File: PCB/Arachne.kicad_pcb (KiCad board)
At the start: 2 copper layers, 100 x 100 mm, 276 parts, among them J201 SW2, J301 SW2, J401 SW2, J501 SW2, J601 SW2, J701 SW2, J801 V_IN, J901 USB_B, J902 PROG_CONN_STM_6p, J903 DBG_UART, M201 Stepper_Motor_bipolar, M301 Stepper_Motor_bipolar, M401 Stepper_Motor_bipolar, M501 Stepper_Motor_bipolar, M601 Stepper_Motor_bipolar, M701 Stepper_Motor_bipolar, Q801 AOD4189, SW101 SW_Push, U101 STM32L452CEUx, U102 WS2818B, U201 L6470_HTSSOP28, U301 L6470_HTSSOP28, U401 L6470_HTSSOP28, U501 L6470_HTSSOP28, U601 L6470_HTSSOP28, U701 L6470_HTSSOP28, U801 ACS712xLCTR-20A, U802 NCP1117-5.0_SOT223, U803 L5973D, U804 NCP1117-3.3_SOT223, U901 USBLC6-2SC6

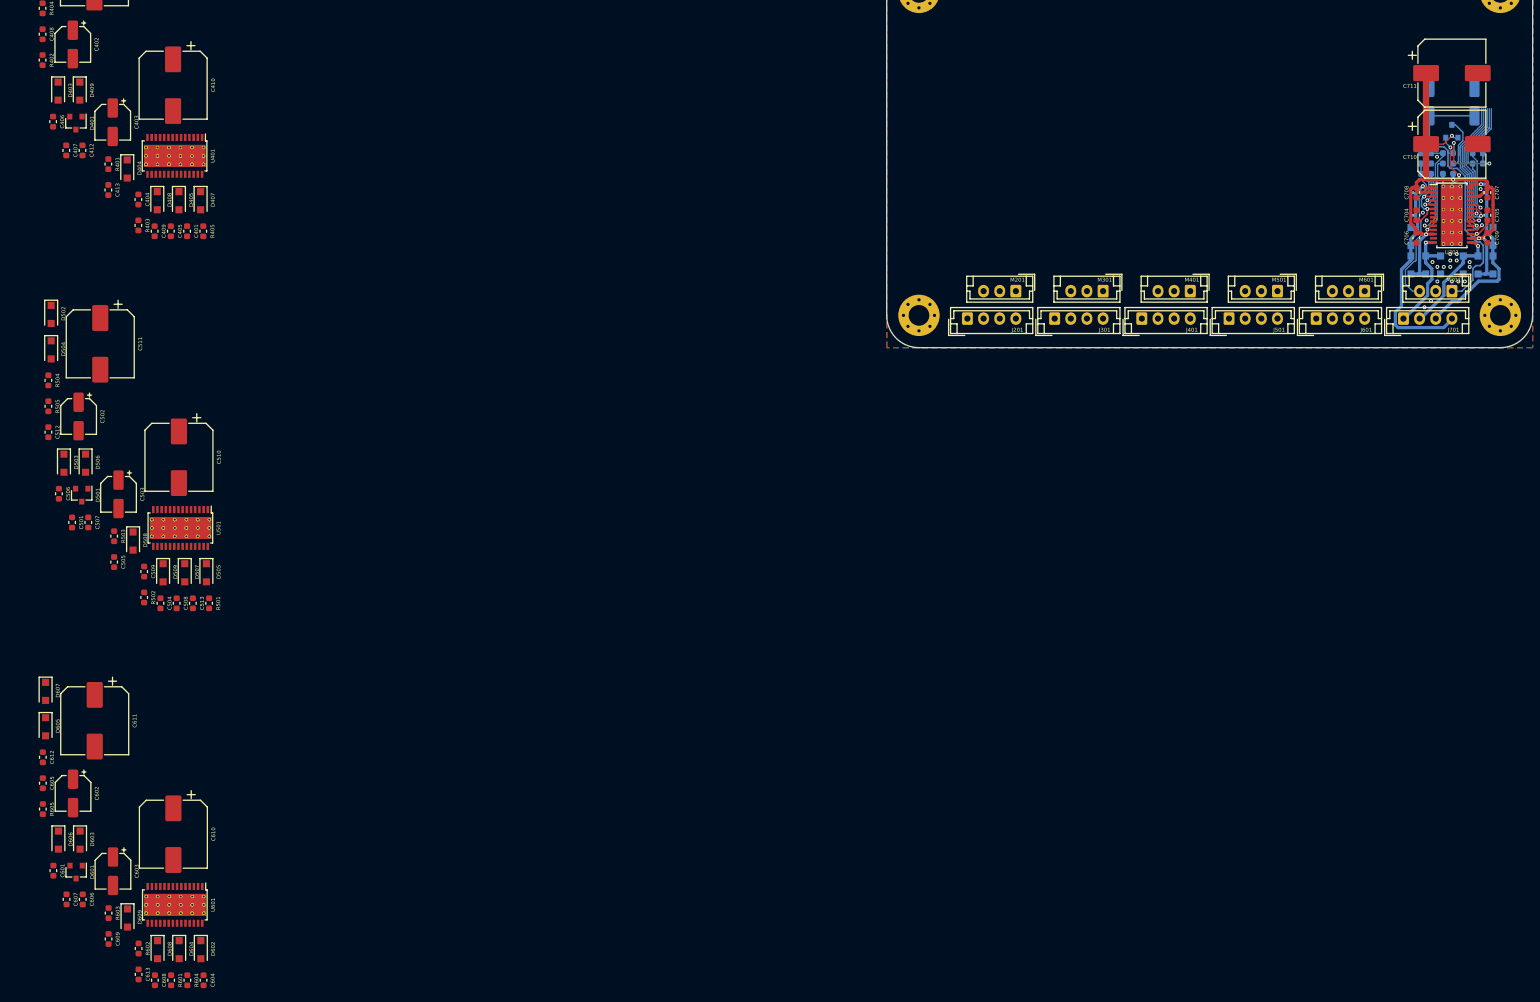
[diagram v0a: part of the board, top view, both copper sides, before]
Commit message: PCB: route driver number 5 (layout replication of 6 with modifications)
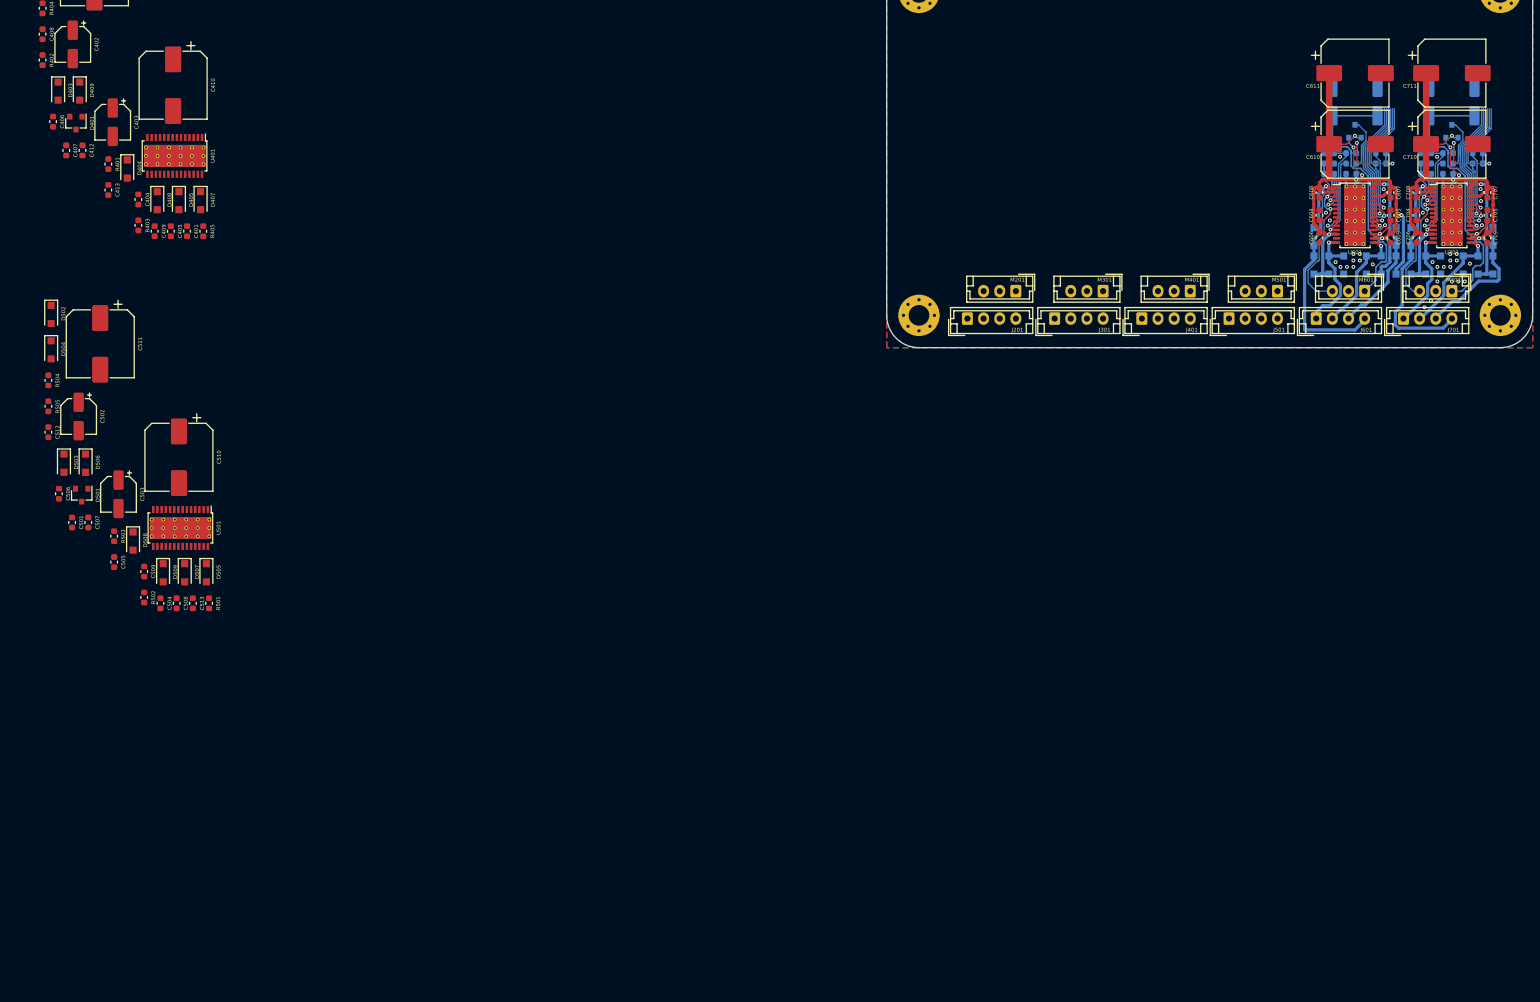
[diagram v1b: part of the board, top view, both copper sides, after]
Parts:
- C601, C602, C603, C612, C613, D601, D602, D603, D604, D605, D606, D607, D608, D609, R601, R602, R603, R604, R605: moved to B.Cu
- moved C607 232.3 mm to (178.0, 126.0)
- moved D601 228.8 mm to (172.5, 116.5), turned to 90 degrees
- moved C602 228.6 mm to (176.0, 111.9), turned to 90 degrees
- moved C601 228.0 mm to (171.9, 123.1), turned to 0 degrees
- moved R602 227.5 mm to (176.5, 121.5), turned to 180 degrees
- moved R601 226.9 mm to (176.5, 119.9), turned to 180 degrees
- moved C605 226.4 mm to (178.0, 129.5), turned to 90 degrees
- moved C609 226.2 mm to (178.0, 133.0)
- moved R603 225.5 mm to (171.9, 119.9), turned to 180 degrees
- moved C603 223.2 mm to (169.0, 111.9), turned to 90 degrees
- moved C613 223.0 mm to (168.5, 121.5), turned to 0 degrees
- moved C612 222.4 mm to (171.9, 121.5), turned to 180 degrees
- moved R605 222.1 mm to (168.5, 123.1), turned to 0 degrees
- moved D608 221.3 mm to (178.8, 132.8), turned to 90 degrees
- moved D606 221.2 mm to (174.2, 137.2)
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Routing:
- net VMOT: track 82.7 -> 174.5 mm, vias 4 -> 9
- net +3V3: track 78.7 -> 155.8 mm, vias 5 -> 10
- net Net-(D605-Pad2): track 0.00 -> 35.8 mm, vias 0 -> 1
- net Net-(D604-Pad2): track 0.00 -> 27.4 mm, vias 0 -> 1
- net /SPI_MISO: track 25.8 -> 51.5 mm, vias 1 -> 2
- net Net-(C613-Pad1): track 0.00 -> 24.8 mm
- net /CS_5: track 0.00 -> 22.0 mm, vias 0 -> 1
- net /SPI_MOSI: track 21.4 -> 42.8 mm, vias 1 -> 2
- net /SPI_SCK: track 21.4 -> 42.8 mm, vias 1 -> 2
- net Net-(C601-Pad1): track 0.00 -> 21.0 mm, vias 0 -> 3
- net /BUSY_5: track 0.00 -> 19.4 mm, vias 0 -> 1
- net /FLAG_5: track 0.00 -> 18.8 mm, vias 0 -> 1
- net Net-(D603-Pad2): track 0.00 -> 18.2 mm, vias 0 -> 1
- net Net-(D602-Pad2): track 0.00 -> 17.4 mm, vias 0 -> 1
- net Net-(C612-Pad2): track 0.00 -> 12.8 mm, vias 0 -> 1
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
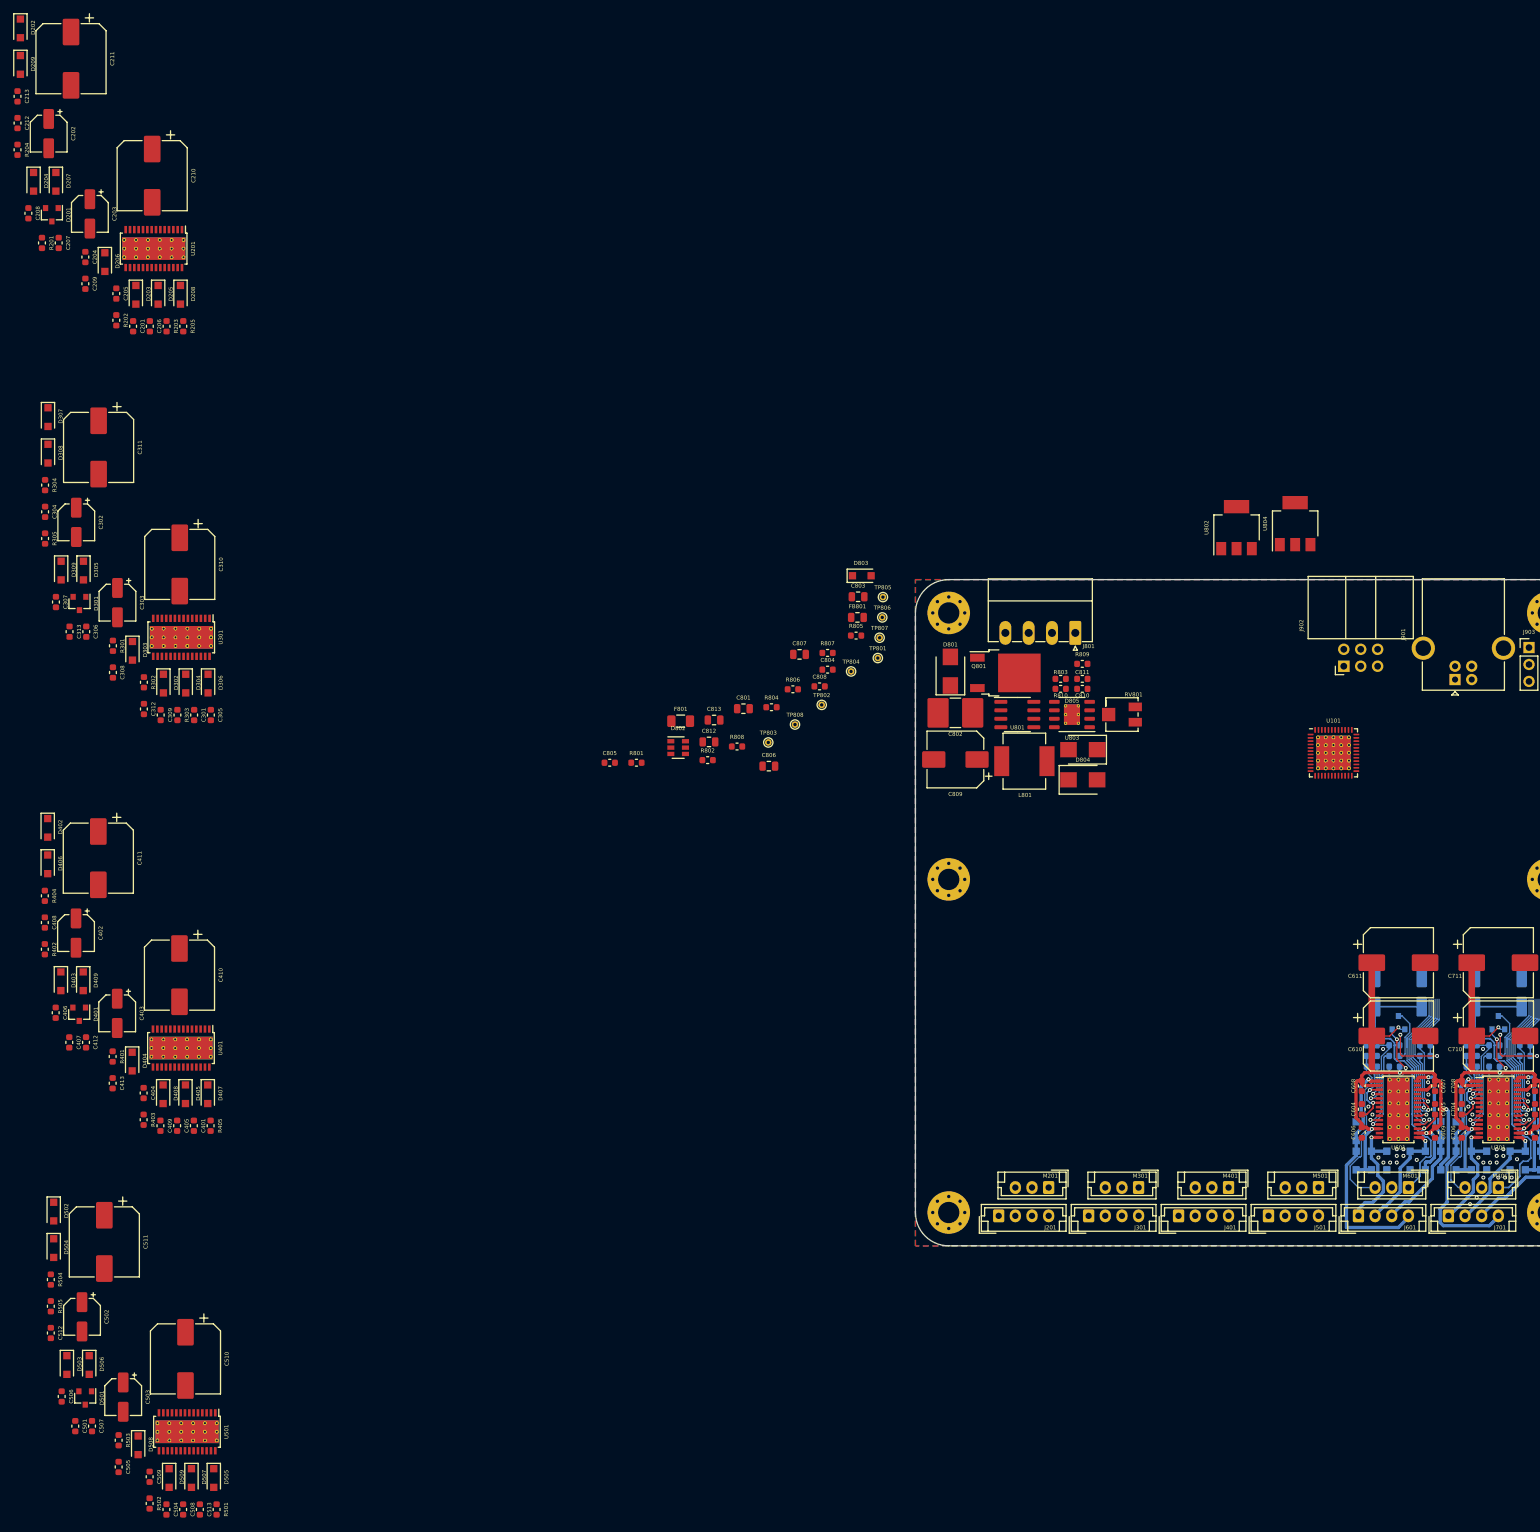
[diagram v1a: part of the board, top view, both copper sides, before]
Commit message: PCB: add routing of remaining driver (1-4)
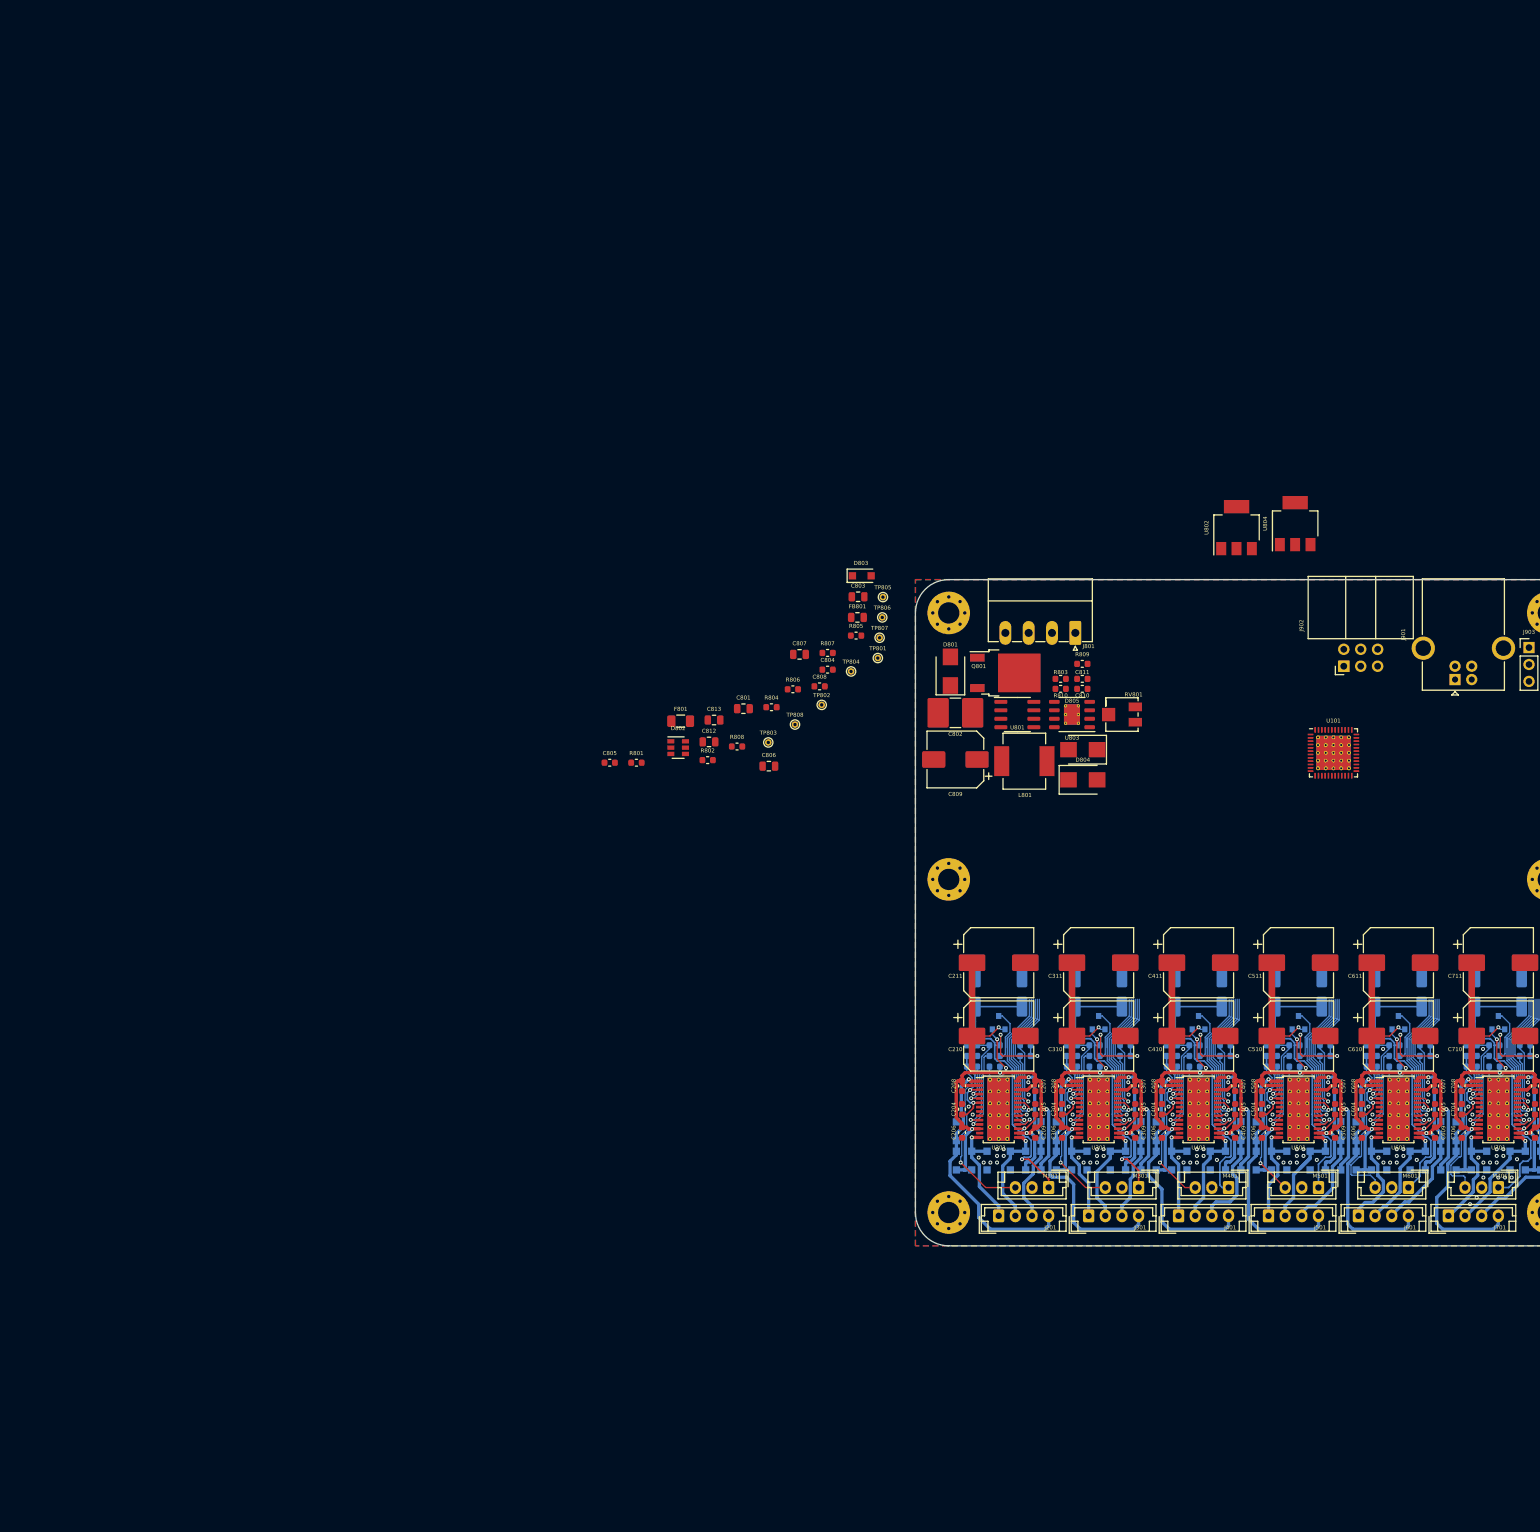
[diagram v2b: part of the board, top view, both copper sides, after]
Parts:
- C201, C202, C203, C212, C213, C301, C302, C303, C312, C313, C401, C402, C403, C412, C413, C501, C502, C503, C512, C513, D201, D202, D203, D204, D205, D206, D207, D208, D209, D301, D302, D303, D304, D305, D306, D307, D308, D309, D401, D402, D403, D404, D405, D406, D407, D408, D409, D501, D502, D503, D504, D505, D506, D507, D508, D509, R201, R202, R203, R204, R205, R301, R302, R303, R304, R305, R401, R402, R403, R404, R405, R501, R502, R503, R504, R505: moved to B.Cu
- moved D202 227.3 mm to (116.5, 137.2), turned to 90 degrees
- moved D209 213.0 mm to (106.2, 132.8), turned to 90 degrees
- moved D204 210.8 mm to (118.8, 137.2), turned to 90 degrees
- moved C213 203.2 mm to (108.5, 121.5), turned to 0 degrees
- moved C212 202.8 mm to (111.9, 121.5), turned to 180 degrees
- moved D207 202.8 mm to (110.8, 137.2)
- moved R204 196.5 mm to (108.5, 119.9), turned to 180 degrees
- moved C202 194.8 mm to (116.0, 111.9), turned to 90 degrees
- moved C211 194.4 mm to (112.5, 107.5), turned to 0 degrees
- moved C207 193.7 mm to (118.0, 126.0)
- moved D504 193.6 mm to (163.8, 137.2), turned to 90 degrees
- moved C507 193.5 mm to (163.0, 126.0)
- moved D308 193.0 mm to (133.8, 132.8), turned to 90 degrees
- moved C502 192.4 mm to (161.0, 111.9), turned to 90 degrees
- moved C208 191.8 mm to (107.0, 126.0)
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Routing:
- net VMOT: track 174.5 -> 546.5 mm, vias 9 -> 29
- net +3V3: track 155.8 -> 466.4 mm, vias 10 -> 32
- net /SPI_MISO: track 51.5 -> 154.6 mm, vias 2 -> 6
- net /SPI_MOSI: track 42.8 -> 128.5 mm, vias 2 -> 6
- net /SPI_SCK: track 42.8 -> 128.5 mm, vias 2 -> 6
- net Net-(D305-Pad2): track 0.00 -> 39.1 mm, vias 0 -> 1
- net Net-(D205-Pad2): track 0.00 -> 38.6 mm, vias 0 -> 1
- net Net-(D405-Pad2): track 0.00 -> 37.6 mm, vias 0 -> 1
- net Net-(D505-Pad2): track 0.00 -> 37.1 mm, vias 0 -> 1
- net Net-(D404-Pad2): track 0.00 -> 27.6 mm, vias 0 -> 1
- net Net-(C213-Pad1): track 0.00 -> 27.0 mm, vias 0 -> 1
- net Net-(D504-Pad2): track 0.00 -> 27.0 mm, vias 0 -> 1
- net Net-(D204-Pad2): track 0.00 -> 25.6 mm, vias 0 -> 1
- net Net-(C313-Pad1): track 0.00 -> 25.5 mm, vias 0 -> 1
- net Net-(D304-Pad2): track 0.00 -> 25.2 mm, vias 0 -> 1
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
